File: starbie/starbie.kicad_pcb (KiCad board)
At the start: 2 copper layers, 34.5 x 43.5 mm, 8 parts, among them J1 Conn_01x04_Pin, J2 Conn_01x08_Pin, SW1 SW_Push, SW2 SW_Push, U1 XIAO-ESP32-C3-SMD, U2 DHT11

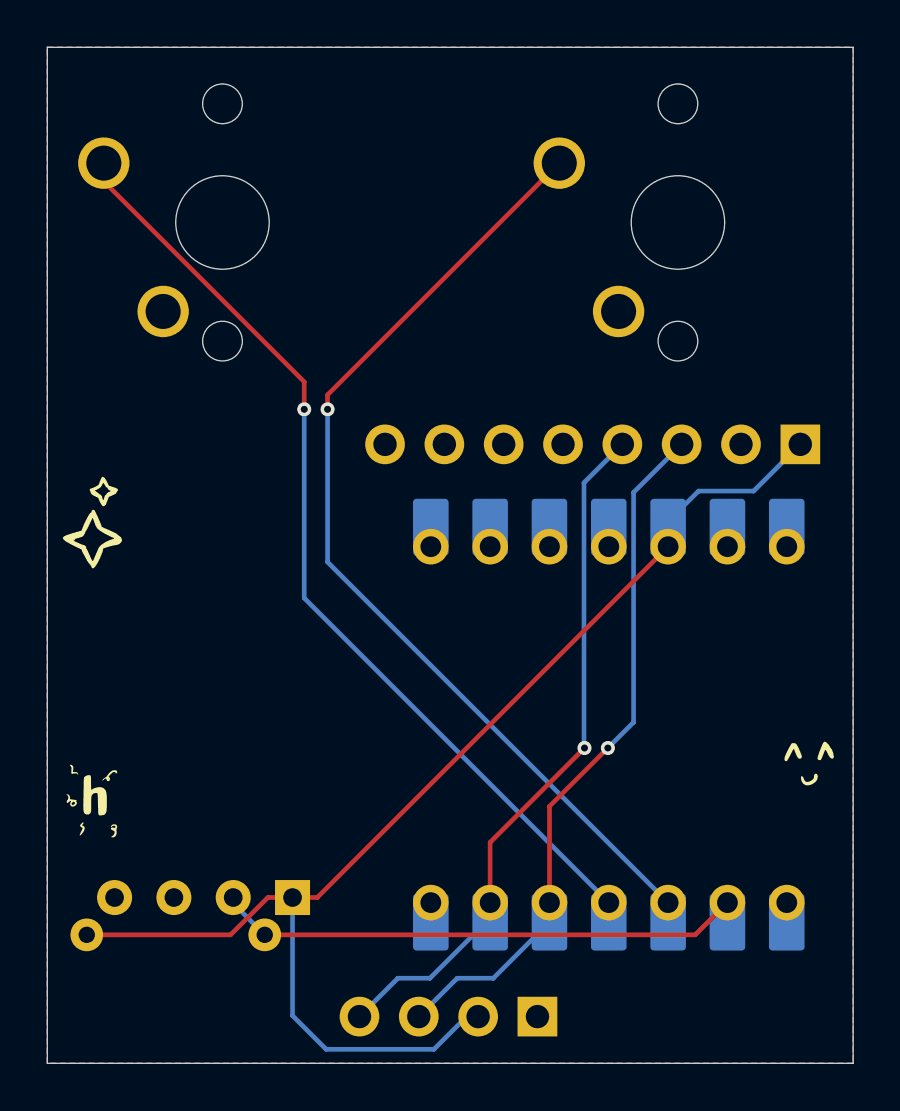
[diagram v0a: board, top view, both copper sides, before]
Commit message: updated schematic and pcb to use SDA and SCL correct way round
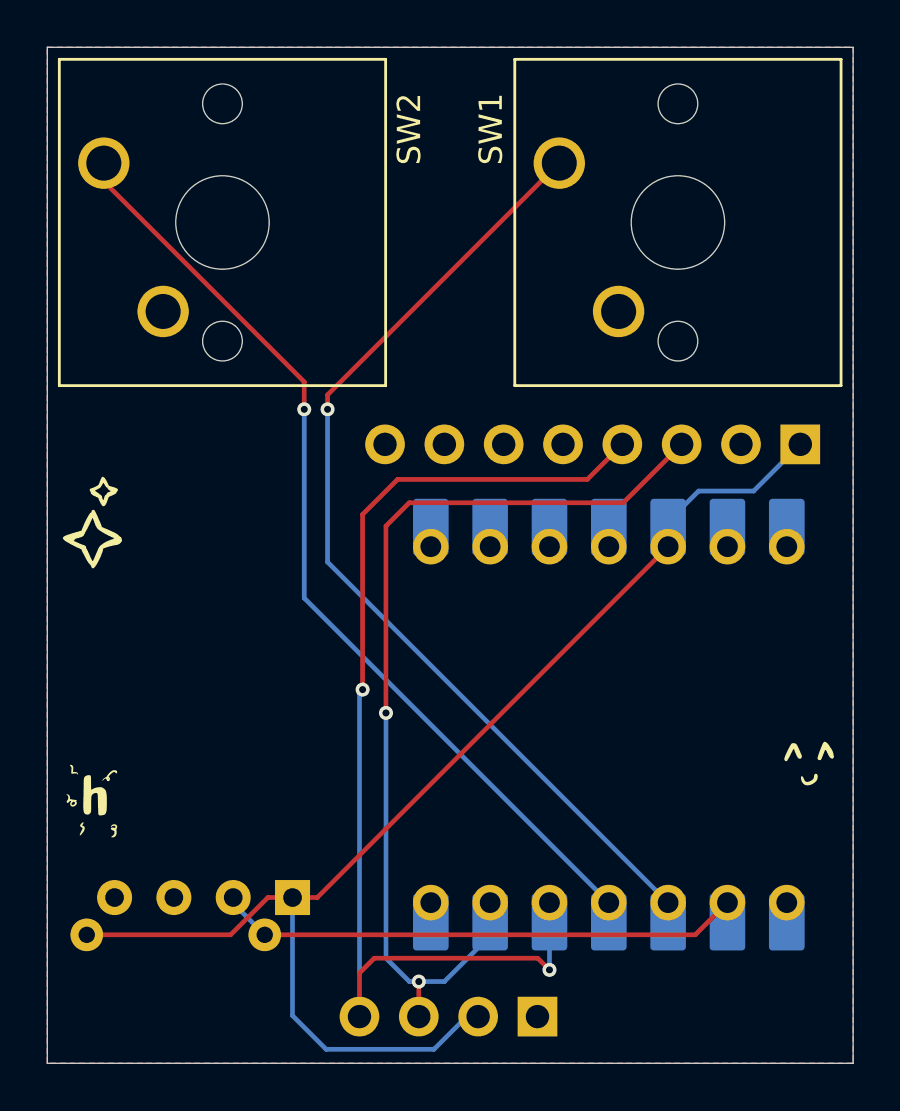
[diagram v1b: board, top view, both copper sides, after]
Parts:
- SW1, SW2: footprint Footprints:SW_Cherry_MX_1.00u -> Button_Switch_Keyboard:SW_Cherry_MX_1.00u_PCB
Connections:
- U1 pad 5: /SCL -> /SDA
- U1 pad 6: /SDA -> /SCL
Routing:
- net /SDA: track 30.0 -> 47.3 mm, vias 1 -> 2
- net /SCL: track 29.2 -> 41.2 mm, vias 1 -> 2
